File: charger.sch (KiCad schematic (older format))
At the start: 0 parts

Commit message: Added Input for coil and battery
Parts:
- added R? (x2): 1M, symbol R
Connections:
- new net +BATT: R?.1
- new net Battery_voltage: R?.1, R?.2
- new net GND: R?.2
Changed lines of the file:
@@
 Comment4 ""
 $EndDescr
+Text HLabel 3150 3600 0    60   Input ~ 0
+Coil_1
+Text HLabel 3150 3800 0    60   Input ~ 0
+Coil_2
+Text HLabel 8800 3950 2    60   Output ~ 0
+Battery_voltage
+$Comp
+L +BATT #PWR?
+U 1 1 5AA78F36
+P 8600 3550
+F 0 "#PWR?" H 8600 3400 50  0001 C CNN
+F 1 "+BATT" H 8600 3690 50  0000 C CNN
+F 2 "" H 8600 3550 50  0001 C CNN
+F 3 "" H 8600 3550 50  0001 C CNN
+	1    8600 3550
+	1    0    0    -1
+$EndComp
+$Comp
+L R R?
+U 1 1 5AA78F4C
+P 8600 3750
+F 0 "R?" V 8680 3750 50  0000 C CNN
+F 1 "1M" V 8600 3750 50  0000 C CNN
+F 2 "" V 8530 3750 50  0001 C CNN
+F 3 "" H 8600 3750 50  0001 C CNN
+	1    8600 3750
+	1    0    0    -1
+$EndComp
+$Comp
+L R R?
+U 1 1 5AA78F86
+P 8600 4150
+F 0 "R?" V 8680 4150 50  0000 C CNN
+F 1 "1M" V 8600 4150 50  0000 C CNN
+F 2 "" V 8530 4150 50  0001 C CNN
+F 3 "" H 8600 4150 50  0001 C CNN
+	1    8600 4150
+	1    0    0    -1
+$EndComp
+$Comp
+L GND #PWR?
+U 1 1 5AA78FC5
+P 8600 4350
+F 0 "#PWR?" H 8600 4100 50  0001 C CNN
+F 1 "GND" H 8600 4200 50  0000 C CNN
+F 2 "" H 8600 4350 50  0001 C CNN
+F 3 "" H 8600 4350 50  0001 C CNN
+	1    8600 4350
+	1    0    0    -1
+$EndComp
+Wire Wire Line
+	8600 3900 8600 3950
+Wire Wire Line
+	8600 3950 8600 4000
+Wire Wire Line
+	8800 3950 8600 3950
+Connection ~ 8600 3950
+Wire Wire Line
+	8600 4350 8600 4300
+Wire Wire Line
+	8600 3550 8600 3600
 $EndSCHEMATC

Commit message: Started working on the charger
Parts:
- added C?: 2u2 6V3, symbol C
- added C? (x2): 10nF 10V, symbol C
- added C? (x2): 22nF 25V, symbol C
- added C? (x2): 470nF 25V, symbol C
- added D?: LED, symbol LED
- added IC?: BQ51050B, lakotamm-miscellaneous:bq5105x_PVQFN_N20, symbol BQ5105xB/QFN
- added R?: R, symbol R
- added R?: 1k2, symbol R
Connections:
- net labels added: VDD, ~CHARGING, ~CHG
- wire segments 5 -> 46
- no-connect marks 0 -> 2
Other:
- note added: "Make sure there is no leak to 2V5 here through the MCU!!!\n"
- note added: "Max 15mA\n"
- note added: "change to 47nF \nif loosing communication"
- moved on the sheet: R?

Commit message: small updates
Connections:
- wire segments 46 -> 37
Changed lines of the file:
@@
 LIBS:power
 LIBS:device
-LIBS:switches
-LIBS:relays
-LIBS:motors
-LIBS:transistors
-LIBS:conn
 LIBS:linear
 LIBS:regul
-LIBS:74xx
-LIBS:cmos4000
 LIBS:adc-dac
 LIBS:memory
@@
 LIBS:digital-audio
 LIBS:philips
-LIBS:display
 LIBS:cypress
 LIBS:siliconi
@@
 LIBS:atmel
 LIBS:contrib
-LIBS:valves
 LIBS:lakotamm-microprocessors
 LIBS:lakotamm-powersupply
@@
 LIBS:lakotamm-transistor
 LIBS:lakotamm-wireless
+LIBS:MCU_ST_STM32
+LIBS:Transistor
+LIBS:Connector
 LIBS:F3K_Battery_manager-cache
 EELAYER 25 0
@@
 $EndComp
 Wire Wire Line
-	8550 4700 8550 4750
-Wire Wire Line
-	8550 4750 8550 4800
+	8550 4700 8550 4800
 Wire Wire Line
 	8750 4750 8550 4750
@@
 	6400 4150 6500 4150
 Wire Wire Line
-	6500 4150 6500 4300
-Wire Wire Line
-	6500 4300 6500 4400
-Wire Wire Line
-	6500 4400 6500 4550
-Wire Wire Line
-	6500 4550 6500 4650
+	6500 4150 6500 4650
 Wire Wire Line
 	6400 4300 6500 4300
@@
 	6400 3250 6500 3250
 Wire Wire Line
-	8350 3800 8550 3800
-Wire Wire Line
-	8550 3800 8700 3800
+	8350 3800 8700 3800
 Connection ~ 8550 3800
 Wire Wire Line
@@
 	5200 3850 4650 3850
 Wire Wire Line
-	4650 3850 4650 4050
-Wire Wire Line
-	4650 4050 4650 4300
-Wire Wire Line
-	4650 4300 4650 4550
+	4650 3850 4650 4550
 Wire Wire Line
 	4650 4550 4750 4550
@@
 	4650 3550 5200 3550
 Wire Wire Line
-	4650 2850 4650 3100
-Wire Wire Line
-	4650 3100 4650 3350
-Wire Wire Line
-	4650 3350 4650 3550
+	4650 2850 4650 3550
 Wire Wire Line
 	5050 2850 5200 2850

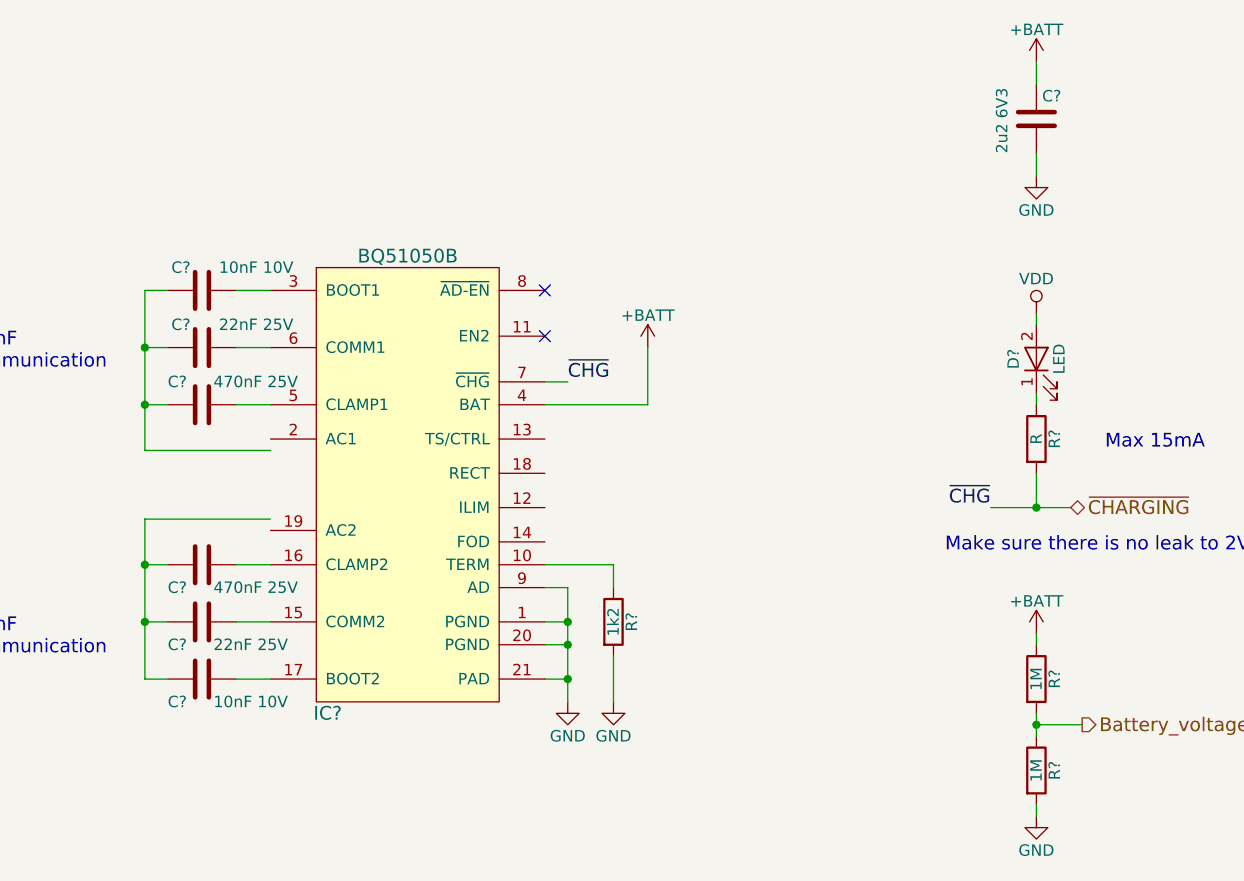
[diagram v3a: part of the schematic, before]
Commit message: added few MPNs
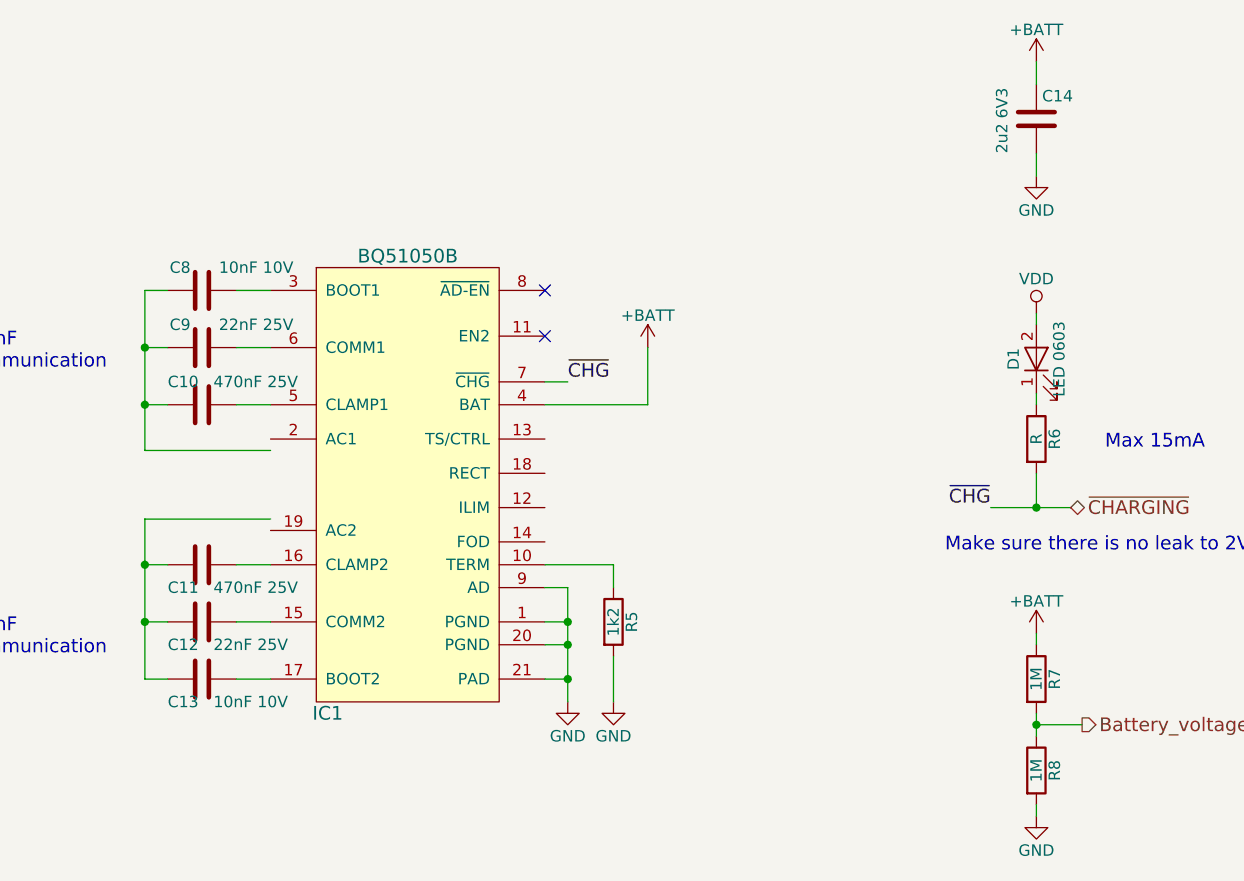
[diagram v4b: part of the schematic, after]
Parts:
- D1: renamed from D?; value LED -> LED 0603; footprint (none) -> Diodes_SMD:D_0603; MPN (none) -> QBLP617-R
- gave numbers to parts that had none: 12
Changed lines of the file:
@@
 Battery_voltage
 $Comp
-L +BATT #PWR?
+L +BATT #PWR42
 U 1 1 5AA78F36
 P 8550 4350
-F 0 "#PWR?" H 8550 4200 50  0001 C CNN
+F 0 "#PWR42" H 8550 4200 50  0001 C CNN
 F 1 "+BATT" H 8550 4490 50  0000 C CNN
 F 2 "" H 8550 4350 50  0001 C CNN
@@
 $EndComp
 $Comp
-L R R?
+L R R7
 U 1 1 5AA78F4C
 P 8550 4550
-F 0 "R?" V 8630 4550 50  0000 C CNN
+F 0 "R7" V 8630 4550 50  0000 C CNN
 F 1 "1M" V 8550 4550 50  0000 C CNN
 F 2 "" V 8480 4550 50  0001 C CNN
@@
 $EndComp
 $Comp
-L R R?
+L R R8
 U 1 1 5AA78F86
 P 8550 4950
-F 0 "R?" V 8630 4950 50  0000 C CNN
+F 0 "R8" V 8630 4950 50  0000 C CNN
 F 1 "1M" V 8550 4950 50  0000 C CNN
 F 2 "" V 8480 4950 50  0001 C CNN
@@
 $EndComp
 $Comp
-L GND #PWR?
+L GND #PWR43
 U 1 1 5AA78FC5
 P 8550 5150
-F 0 "#PWR?" H 8550 4900 50  0001 C CNN
+F 0 "#PWR43" H 8550 4900 50  0001 C CNN
 F 1 "GND" H 8550 5000 50  0000 C CNN
 F 2 "" H 8550 5150 50  0001 C CNN
@@
 $EndComp
 $Comp
-L BQ5105xB/QFN IC?
+L BQ5105xB/QFN IC1
 U 1 1 5AA84E21
 P 5800 3700
-F 0 "IC?" H 5450 2700 60  0000 C CNN
+F 0 "IC1" H 5450 2700 60  0000 C CNN
 F 1 "BQ51050B" H 5800 4700 60  0000 C CNN
 F 2 "lakotamm-miscellaneous:bq5105x_PVQFN_N20" H 5800 2550 60  0001 C CNN
@@
 $EndComp
 $Comp
-L GND #PWR?
+L GND #PWR36
 U 1 1 5AA85C8F
 P 6500 4650
-F 0 "#PWR?" H 6500 4400 50  0001 C CNN
+F 0 "#PWR36" H 6500 4400 50  0001 C CNN
 F 1 "GND" H 6500 4500 50  0000 C CNN
 F 2 "" H 6500 4650 50  0001 C CNN
@@
 $EndComp
 $Comp
-L +BATT #PWR?
+L +BATT #PWR38
 U 1 1 5AA85D44
 P 6850 3100
-F 0 "#PWR?" H 6850 2950 50  0001 C CNN
+F 0 "#PWR38" H 6850 2950 50  0001 C CNN
 F 1 "+BATT" H 6850 3240 50  0000 C CNN
 F 2 "" H 6850 3100 50  0001 C CNN
@@
 NoConn ~ 6400 2850
 $Comp
-L R R?
+L R R6
 U 1 1 5AA85E7B
 P 8550 3500
-F 0 "R?" V 8630 3500 50  0000 C CNN
+F 0 "R6" V 8630 3500 50  0000 C CNN
 F 1 "R" V 8550 3500 50  0000 C CNN
 F 2 "" V 8480 3500 50  0001 C CNN
@@
 $EndComp
 $Comp
-L LED D?
+L LED D1
 U 1 1 5AA863C5
 P 8550 3150
-F 0 "D?" H 8550 3250 50  0000 C CNN
-F 1 "LED" H 8550 3050 50  0000 C CNN
-F 2 "" H 8550 3150 50  0001 C CNN
-F 3 "" H 8550 3150 50  0001 C CNN
+F 0 "D1" H 8550 3250 50  0000 C CNN
+F 1 "LED 0603" H 8550 3050 50  0000 C CNN
+F 2 "Diodes_SMD:D_0603" H 8550 3150 50  0001 C CNN
+F 3 "http://www.qt-brightek.com/datasheet/QBLP617_series.pdf" H 8550 3150 50  0001 C CNN
+F 4 "QBLP617-R" H 8550 3150 60  0001 C CNN "MPN"
 	1    8550 3150
 	0    -1   -1   0
@@
 ~CHARGING
 $Comp
-L R R?
+L R R5
 U 1 1 5AA86C77
 P 6700 4300
-F 0 "R?" V 6780 4300 50  0000 C CNN
+F 0 "R5" V 6780 4300 50  0000 C CNN
 F 1 "1k2" V 6700 4300 50  0000 C CNN
 F 2 "" V 6630 4300 50  0001 C CNN
@@
 $EndComp
 $Comp
-L GND #PWR?
+L GND #PWR37
 U 1 1 5AA86D68
 P 6700 4650
-F 0 "#PWR?" H 6700 4400 50  0001 C CNN
+F 0 "#PWR37" H 6700 4400 50  0001 C CNN
 F 1 "GND" H 6700 4500 50  0000 C CNN
 F 2 "" H 6700 4650 50  0001 C CNN
@@
 $EndComp
 $Comp
-L +BATT #PWR?
+L +BATT #PWR39
 U 1 1 5AA87B72
 P 8550 1850
-F 0 "#PWR?" H 8550 1700 50  0001 C CNN
+F 0 "#PWR39" H 8550 1700 50  0001 C CNN
 F 1 "+BATT" H 8550 1990 50  0000 C CNN
 F 2 "" H 8550 1850 50  0001 C CNN
@@
 $EndComp
 $Comp
-L C C?
+L C C14
 U 1 1 5AA87B8B
 P 8550 2100
-F 0 "C?" H 8575 2200 50  0000 L CNN
+F 0 "C14" H 8575 2200 50  0000 L CNN
 F 1 "2u2 6V3" V 8400 1950 50  0000 L CNN
 F 2 "" H 8588 1950 50  0001 C CNN
@@
 $EndComp
 $Comp
-L GND #PWR?
+L GND #PWR40
 U 1 1 5AA87C01
 P 8550 2350
-F 0 "#PWR?" H 8550 2100 50  0001 C CNN
+F 0 "#PWR40" H 8550 2100 50  0001 C CNN
 F 1 "GND" H 8550 2200 50  0000 C CNN
 F 2 "" H 8550 2350 50  0001 C CNN
@@
 $EndComp
 $Comp
-L C C?
+L C C8
 U 1 1 5AA87D3B
 P 4900 2850
-F 0 "C?" V 5000 2900 50  0000 L CNN
+F 0 "C8" V 5000 2900 50  0000 L CNN
 F 1 "10nF 10V" V 5000 2450 50  0000 L CNN
 F 2 "" H 4938 2700 50  0001 C CNN
@@
 $EndComp
 $Comp
-L C C?
+L C C13
 U 1 1 5AA87DF5
 P 4900 4550
-F 0 "C?" V 5000 4400 50  0000 L CNN
+F 0 "C13" V 5000 4400 50  0000 L CNN
 F 1 "10nF 10V" V 5000 4600 50  0000 L CNN
 F 2 "" H 4938 4400 50  0001 C CNN
@@
 $EndComp
 $Comp
-L C C?
+L C C12
 U 1 1 5AA882B8
 P 4900 4300
-F 0 "C?" V 5000 4150 50  0000 L CNN
+F 0 "C12" V 5000 4150 50  0000 L CNN
 F 1 "22nF 25V" V 5000 4350 50  0000 L CNN
 F 2 "" H 4938 4150 50  0001 C CNN
@@
 change to 47nF \nif loosing communication
 $Comp
-L C C?
+L C C11
 U 1 1 5AA8A27D
 P 4900 4050
-F 0 "C?" V 5000 3900 50  0000 L CNN
+F 0 "C11" V 5000 3900 50  0000 L CNN
 F 1 "470nF 25V" V 5000 4100 50  0000 L CNN
 F 2 "" H 4938 3900 50  0001 C CNN
@@
 $EndComp
 $Comp
-L C C?
+L C C10
 U 1 1 5AA8A4C2
 P 4900 3350
-F 0 "C?" V 4800 3200 50  0000 L CNN
+F 0 "C10" V 4800 3200 50  0000 L CNN
 F 1 "470nF 25V" V 4800 3400 50  0000 L CNN
 F 2 "" H 4938 3200 50  0001 C CNN
@@
 $EndComp
 $Comp
-L C C?
+L C C9
 U 1 1 5AA88198
 P 4900 3100
-F 0 "C?" V 5000 3150 50  0000 L CNN
+F 0 "C9" V 5000 3150 50  0000 L CNN
 F 1 "22nF 25V" V 5000 2700 50  0000 L CNN
 F 2 "" H 4938 2950 50  0001 C CNN
@@
 Make sure there is no leak to 2V5 here through the MCU!!!\n
 $Comp
-L VDD #PWR?
+L VDD #PWR41
 U 1 1 5AA8B638
 P 8550 2950
-F 0 "#PWR?" H 8550 2800 50  0001 C CNN
+F 0 "#PWR41" H 8550 2800 50  0001 C CNN
 F 1 "VDD" H 8550 3100 50  0000 C CNN
 F 2 "" H 8550 2950 50  0001 C CNN

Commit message: Progress on the charging circuit
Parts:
- added C? (x2): C, symbol C
- added C? (x2): 4u7 16V, symbol C
- added C?: 470nF 25V, symbol C
- added R?: 200R, symbol R
- added R?: R, symbol R
- added R?: 10K, symbol R
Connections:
- net labels added: Charge_control, ILIM, TS/CTRL, Thermistor, Thermistor_OFF
- wire segments 37 -> 59
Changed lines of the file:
@@
 $Descr A4 11693 8268
 encoding utf-8
-Sheet 3 4
+Sheet 4 4
 Title ""
 Date ""
@@
 Comment4 ""
 $EndDescr
-Text HLabel 3250 3550 0    60   Input ~ 0
+Text HLabel 3250 3500 0    60   Input ~ 0
 Coil_1
-Text HLabel 3250 3850 0    60   Input ~ 0
+Text HLabel 3250 3900 0    60   Input ~ 0
 Coil_2
 Text HLabel 8750 4750 2    60   Output ~ 0
@@
 P 8550 3150
 F 0 "D1" H 8550 3250 50  0000 C CNN
-F 1 "LED 0603" H 8550 3050 50  0000 C CNN
+F 1 "LED 0603" H 8550 3000 50  0000 C CNN
 F 2 "Diodes_SMD:D_0603" H 8550 3150 50  0001 C CNN
 F 3 "http://www.qt-brightek.com/datasheet/QBLP617_series.pdf" H 8550 3150 50  0001 C CNN
@@
 Text Label 8350 3800 2    60   ~ 0
 ~CHG
-Text HLabel 8700 3800 2    60   BiDi ~ 0
+Text HLabel 8700 3800 2    60   Output ~ 0
 ~CHARGING
 $Comp
@@
 U 1 1 5AA87DF5
 P 4900 4550
-F 0 "C13" V 5000 4400 50  0000 L CNN
+F 0 "C13" V 5000 4350 50  0000 L CNN
 F 1 "10nF 10V" V 5000 4600 50  0000 L CNN
 F 2 "" H 4938 4400 50  0001 C CNN
@@
 U 1 1 5AA882B8
 P 4900 4300
-F 0 "C12" V 5000 4150 50  0000 L CNN
+F 0 "C12" V 5000 4100 50  0000 L CNN
 F 1 "22nF 25V" V 5000 4350 50  0000 L CNN
 F 2 "" H 4938 4150 50  0001 C CNN
@@
 U 1 1 5AA8A27D
 P 4900 4050
-F 0 "C11" V 5000 3900 50  0000 L CNN
+F 0 "C11" V 5000 3850 50  0000 L CNN
 F 1 "470nF 25V" V 5000 4100 50  0000 L CNN
 F 2 "" H 4938 3900 50  0001 C CNN
@@
 U 1 1 5AA8A4C2
 P 4900 3350
-F 0 "C10" V 4800 3200 50  0000 L CNN
+F 0 "C10" V 4800 3150 50  0000 L CNN
 F 1 "470nF 25V" V 4800 3400 50  0000 L CNN
 F 2 "" H 4938 3200 50  0001 C CNN
@@
 	5050 4550 5200 4550
 Wire Wire Line
-	5200 3850 4650 3850
-Wire Wire Line
-	4650 3850 4650 4550
-Wire Wire Line
 	4650 4550 4750 4550
 Wire Wire Line
-	4650 3550 5200 3550
-Wire Wire Line
-	4650 2850 4650 3550
-Wire Wire Line
 	5050 2850 5200 2850
 Wire Wire Line
@@
 	5050 4300 5200 4300
 Wire Wire Line
-	4750 4300 4650 4300
+	4650 4300 4750 4300
 Connection ~ 4650 4300
 Wire Wire Line
@@
 	5200 3350 5050 3350
 Wire Wire Line
-	4750 3350 4650 3350
+	4650 3350 4750 3350
 Connection ~ 4650 3350
 Text Notes 8150 4000 0    60   ~ 0
@@
 Text Notes 8850 3550 0    60   ~ 0
 Max 15mA\n
+$Comp
+L C C?
+U 1 1 5AB055C0
+P 4250 3700
+F 0 "C?" V 4150 3550 50  0000 L CNN
+F 1 "C" H 4350 3800 50  0000 L CNN
+F 2 "" H 4288 3550 50  0001 C CNN
+F 3 "" H 4250 3700 50  0001 C CNN
+	1    4250 3700
+	-1   0    0    1
+$EndComp
+$Comp
+L C C?
+U 1 1 5AB0567E
+P 3600 3500
+F 0 "C?" H 3625 3600 50  0000 L CNN
+F 1 "C" H 3625 3400 50  0000 L CNN
+F 2 "" H 3638 3350 50  0001 C CNN
+F 3 "" H 3600 3500 50  0001 C CNN
+	1    3600 3500
+	0    1    1    0
+$EndComp
+Wire Wire Line
+	3250 3500 3450 3500
+Wire Wire Line
+	3750 3500 5200 3500
+Wire Wire Line
+	4250 3500 4250 3550
+Connection ~ 4650 3500
+Connection ~ 4250 3500
+Wire Wire Line
+	3250 3900 5200 3900
+Connection ~ 4650 3900
+Wire Wire Line
+	4250 3850 4250 3900
+Connection ~ 4250 3900
+Wire Wire Line
+	4650 2850 4650 3500
+Wire Wire Line
+	4650 3900 4650 4550
+$Comp
+L R R?
+U 1 1 5AB0687F
+P 6950 4300
+F 0 "R?" V 7030 4300 50  0000 C CNN
+F 1 "200R" V 6950 4300 50  0000 C CNN
+F 2 "" V 6880 4300 50  0001 C CNN
+F 3 "" H 6950 4300 50  0001 C CNN
+	1    6950 4300
+	1    0    0    -1
+$EndComp
+Wire Wire Line
+	6400 3950 6950 3950
+Wire Wire Line
+	6950 3950 6950 4150
+$Comp
+L GND #PWR?
+U 1 1 5AB06991
+P 6950 4650
+F 0 "#PWR?" H 6950 4400 50  0001 C CNN
+F 1 "GND" H 6950 4500 50  0000 C CNN
+F 2 "" H 6950 4650 50  0001 C CNN
+F 3 "" H 6950 4650 50  0001 C CNN
+	1    6950 4650
+	1    0    0    -1
+$EndComp
+Wire Wire Line
+	6950 4450 6950 4650
+Text Label 6500 3800 0    60   ~ 0
+ILIM
+Wire Wire Line
+	6400 3800 6500 3800
+Text Label 6500 3500 0    60   ~ 0
+TS/CTRL
+Wire Wire Line
+	6400 3500 6500 3500
+$Comp
+L C C?
+U 1 1 5AB0745B
+P 7250 4300
+F 0 "C?" H 7275 4400 50  0000 L CNN
+F 1 "4u7 16V" V 7400 4150 50  0000 L CNN
+F 2 "" H 7288 4150 50  0001 C CNN
+F 3 "" H 7250 4300 50  0001 C CNN
+	1    7250 4300
+	1    0    0    -1
+$EndComp
+Wire Wire Line
+	7250 4150 7250 3650
+Wire Wire Line
+	6400 3650 7550 3650
+$Comp
+L GND #PWR?
+U 1 1 5AB07537
+P 7250 4650
+F 0 "#PWR?" H 7250 4400 50  0001 C CNN
+F 1 "GND" H 7250 4500 50  0000 C CNN
+F 2 "" H 7250 4650 50  0001 C CNN
+F 3 "" H 7250 4650 50  0001 C CNN
+	1    7250 4650
+	1    0    0    -1
+$EndComp
+Wire Wire Line
+	7250 4450 7250 4650
+Text Label 6550 1750 2    60   ~ 0
+TS/CTRL
+Text HLabel 6550 2200 0    60   Input ~ 0
+Thermistor
+$Comp
+L C C?
+U 1 1 5AB15596
+P 7550 4300
+F 0 "C?" H 7575 4400 50  0000 L CNN
+F 1 "4u7 16V" V 7700 4150 50  0000 L CNN
+F 2 "" H 7588 4150 50  0001 C CNN
+F 3 "" H 7550 4300 50  0001 C CNN
+	1    7550 4300
+	1    0    0    -1
+$EndComp
+Wire Wire Line
+	7550 3650 7550 4150
+Connection ~ 7250 3650
+$Comp
+L GND #PWR?
+U 1 1 5AB15630
+P 7550 4650
+F 0 "#PWR?" H 7550 4400 50  0001 C CNN
+F 1 "GND" H 7550 4500 50  0000 C CNN
+F 2 "" H 7550 4650 50  0001 C CNN
+F 3 "" H 7550 4650 50  0001 C CNN
+	1    7550 4650
+	1    0    0    -1
+$EndComp
+Wire Wire Line
+	7550 4450 7550 4650
+$Comp
+L R R?
+U 1 1 5AB15ADC
+P 6650 1950
+F 0 "R?" V 6730 1950 50  0000 C CNN
+F 1 "R" V 6650 1950 50  0000 C CNN
+F 2 "" V 6580 1950 50  0001 C CNN
+F 3 "" H 6650 1950 50  0001 C CNN
+	1    6650 1950
+	1    0    0    -1
+$EndComp
+Wire Wire Line
+	6550 1750 7200 1750
+Wire Wire Line
+	6650 1750 6650 1800
+Wire Wire Line
+	6550 2200 6650 2200
+Wire Wire Line
+	6650 2200 6650 2100
+$Comp
+L C C?
+U 1 1 5AB15F72
+P 7100 2050
+F 0 "C?" H 7125 2150 50  0000 L CNN
+F 1 "470nF 25V" H 7125 1950 50  0000 L CNN
+F 2 "" H 7138 1900 50  0001 C CNN
+F 3 "" H 7100 2050 50  0001 C CNN
+	1    7100 2050
+	1    0    0    -1
+$EndComp
+$Comp
+L GND #PWR?
+U 1 1 5AB160F7
+P 7100 2350
+F 0 "#PWR?" H 7100 2100 50  0001 C CNN
+F 1 "GND" H 7100 2200 50  0000 C CNN
+F 2 "" H 7100 2350 50  0001 C CNN
+F 3 "" H 7100 2350 50  0001 C CNN
+	1    7100 2350
+	1    0    0    -1
+$EndComp
+Wire Wire Line
+	7100 1750 7100 1900
+Connection ~ 6650 1750
+Wire Wire Line
+	7100 2200 7100 2350
+$Comp
+L R R?
+U 1 1 5AB17BEE
+P 6850 1950
+F 0 "R?" V 6930 1950 50  0000 C CNN
+F 1 "10K" V 6850 1950 50  0000 C CNN
+F 2 "" V 6780 1950 50  0001 C CNN
+F 3 "" H 6850 1950 50  0001 C CNN
+	1    6850 1950
+	1    0    0    -1
+$EndComp
+Wire Wire Line
+	6850 1800 6850 1750
+Connection ~ 6850 1750
+Text HLabel 7200 1750 2    60   Input ~ 0
+Charge_control
+Connection ~ 7100 1750
+Text HLabel 6550 2350 0    60   Input ~ 0
+Thermistor_OFF
+Wire Wire Line
+	6550 2350 6850 2350
+Wire Wire Line
+	6850 2350 6850 2100
 $EndSCHEMATC
